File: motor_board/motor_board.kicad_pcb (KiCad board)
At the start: 2 copper layers, 57 x 51 mm, 32 parts, among them IC1 TORX1950A_F_, J1 Conn_01x16_Socket, U1 DRV8833PW, U2 DCP3603BCMR, U3 TXS0101DBV, U5 74LVC1GU04

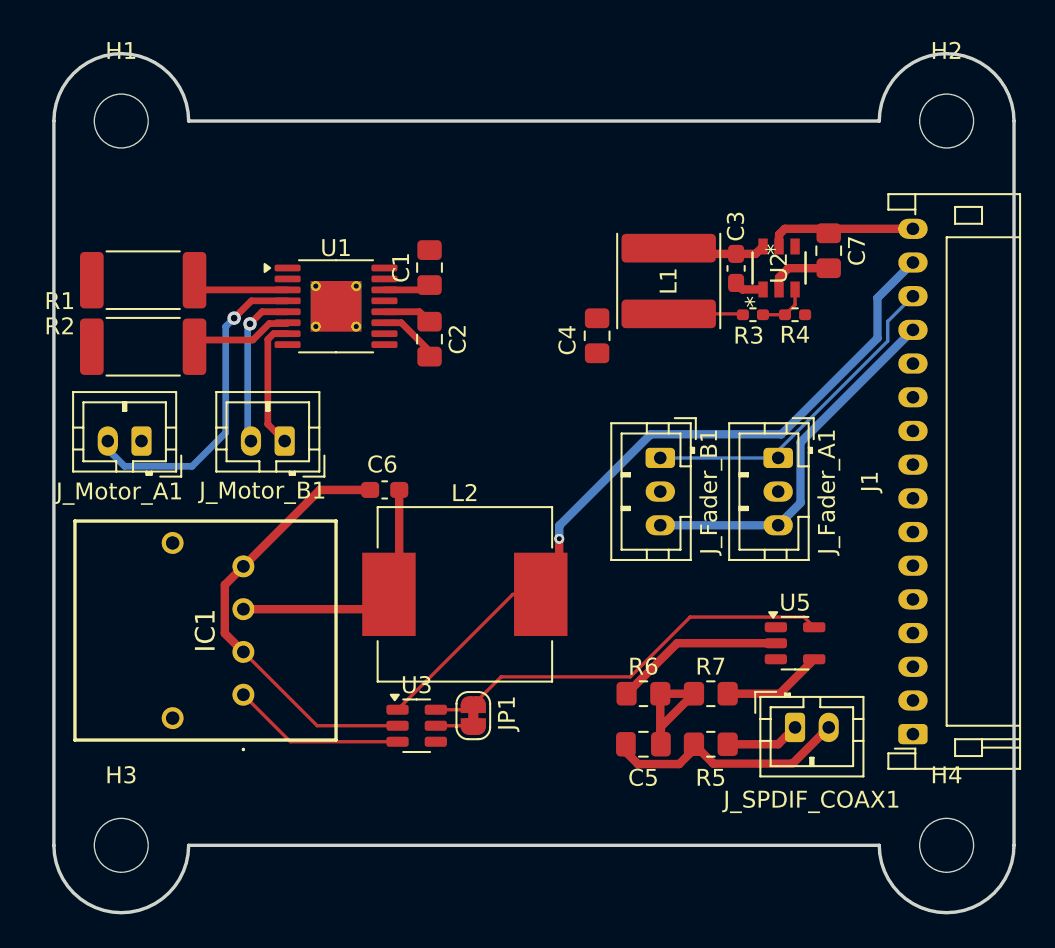
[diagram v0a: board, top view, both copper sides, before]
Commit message: Finished motor board PCB
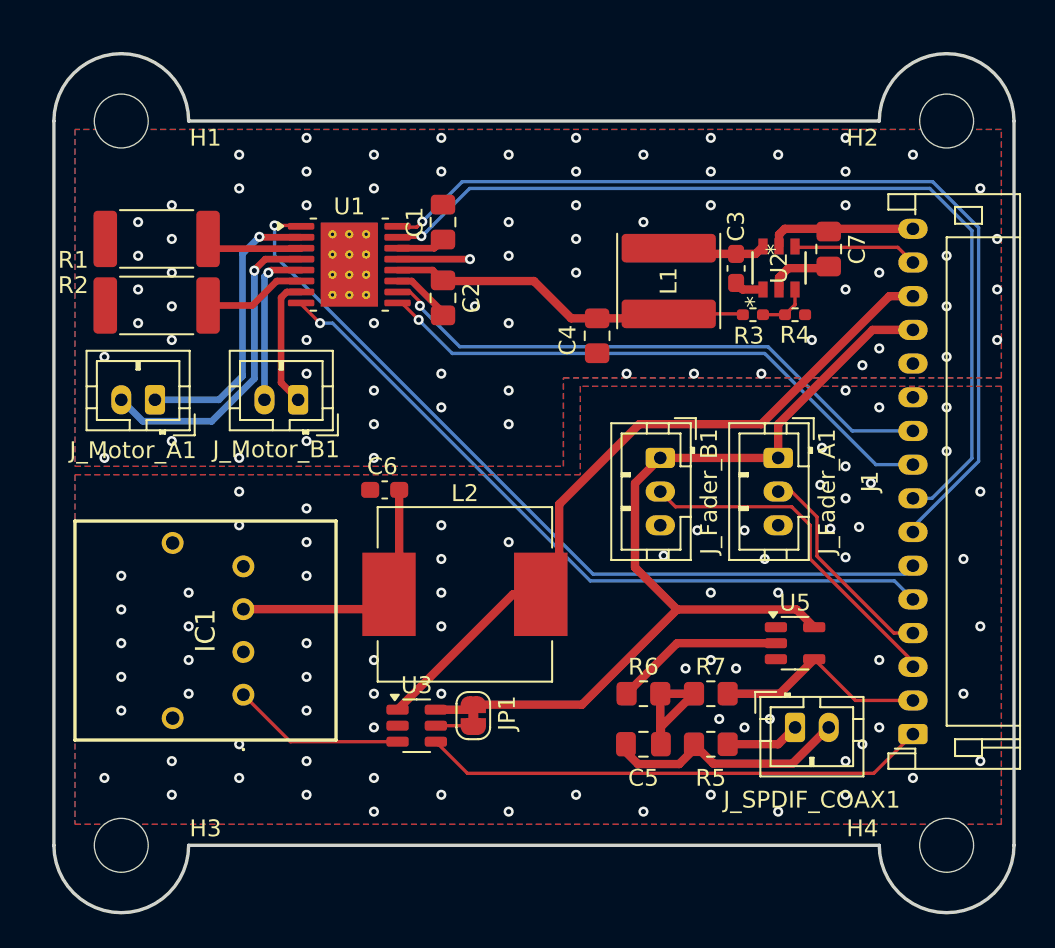
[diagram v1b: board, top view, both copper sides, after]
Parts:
- U1: value DRV8833PW -> DRV8833PWP; footprint Package_SO:TSSOP-16-1EP_4.4x5mm_P0.65mm_EP3x3mm_ThermalVias -> Package_SO:HTSSOP-16-1EP_4.4x5mm_P0.65mm_EP3.4x5mm_Mask2.46x2.31mm_ThermalVias
- moved C1 2.82 mm to (130.1, 90.0)
- moved U1 2.60 mm to (124.5, 92.5)
- moved J_Motor_A1 2.58 mm to (113.0, 100.5)
- moved J_Motor_B1 2.58 mm to (121.5, 100.5)
- moved R1 2.58 mm to (113.1, 91.0)
- moved R2 2.58 mm to (113.1, 95.0)
- moved C2 2.58 mm to (130.1, 94.5)
- moved C7 0.10 mm to (153.0, 91.6)
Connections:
- J1 pad 1: AIN1 -> SPDIFRX_TOS
- J1 pad 10: SPDIFRX_COAX -> BIN2
- J1 pad 11: SPDIFRX_TOS -> GNDD
- J1 pad 13: GNDD -> +3.3V
- J1 pad 14: +3.3V -> +5V
- J1 pad 15: +5V -> EN
- J1 pad 2: AIN2 -> SPDIFRX_COAX
- J1 pad 3: BIN1 -> WIPER_B
- J1 pad 4: BIN2 -> WIPER_A
- J1 pad 7: EN -> AIN1
- J1 pad 8: WIPER_A -> AIN2
- J1 pad 9: WIPER_B -> BIN1
- U1 pad 17: (no net) -> GND
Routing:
- net AIN1: track 0.00 -> 56.5 mm, vias 0 -> 1
- net AIN2: track 0.00 -> 54.3 mm, vias 0 -> 1
- net ~{SLEEP}: track 0.00 -> 49.3 mm, vias 0 -> 1
- net GNDD: track 52.7 -> 4.41 mm, vias 0 -> 76
- net ~{FAULT}: track 0.00 -> 43.7 mm, vias 0 -> 1
- net BIN2: track 0.00 -> 34.7 mm, vias 0 -> 1
- net BIN1: track 0.00 -> 34.6 mm, vias 0 -> 1
- net SPDIFRX_TOS: track 0.00 -> 30.1 mm
- net WIPER_B: track 0.00 -> 20.7 mm
- net Net-(J_Motor_A1-Pin_1): track 0.00 -> 17.0 mm, vias 0 -> 1
- net VDC: track 7.34 -> 21.8 mm
- net WIPER_A: track 0.00 -> 12.8 mm
- net +3.3V: track 44.9 -> 55.3 mm
- net EN: track 0.00 -> 7.39 mm
- net SPDIFRX_COAX: track 5.99 -> 12.9 mm
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- added copper zone on B.Cu, net GND
- added copper zone on F.Cu, net GND
- added copper zone on B.Cu, net GNDD
- added copper zone on F.Cu, net GNDD

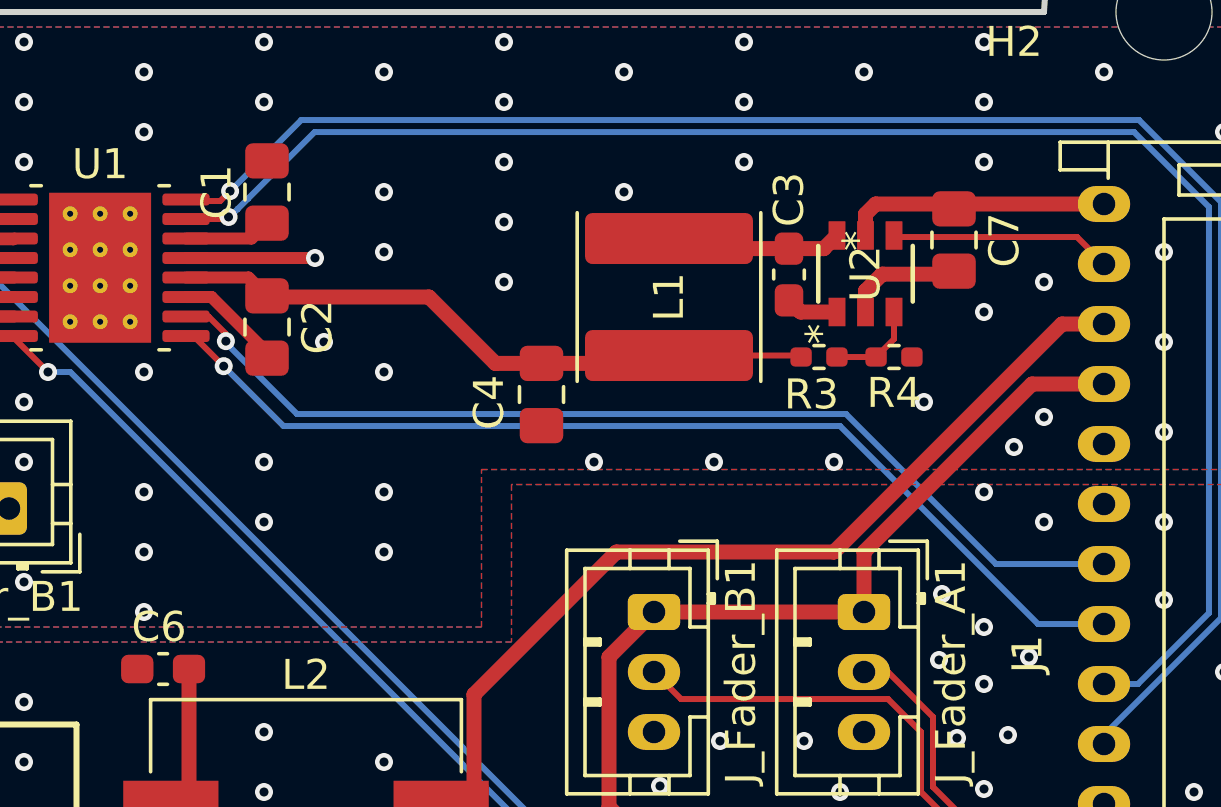
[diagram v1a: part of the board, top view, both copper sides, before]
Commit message: Modified motor_board; larger DC/DC inductor
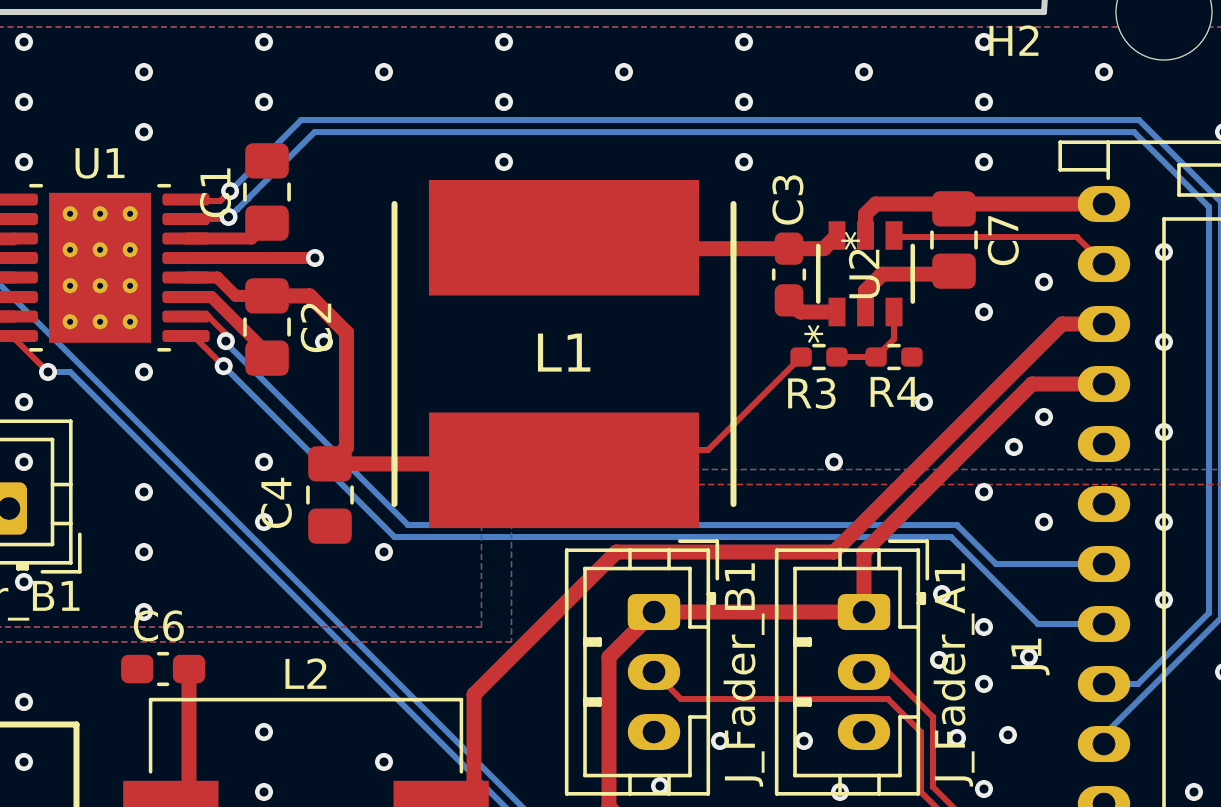
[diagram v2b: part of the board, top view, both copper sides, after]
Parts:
- L1: footprint Inductor_SMD:L_Wuerth_MAPI-5030 -> 744393665033:744393665033
- moved C4 7.81 mm to (132.2, 100.1)
- moved L1 3.98 mm to (140.0, 95.4), turned to 180 degrees
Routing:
- net VDC: track 21.8 -> 28.0 mm
- net SW: track 5.92 -> 9.41 mm
- net GND: vias 69 -> 60
